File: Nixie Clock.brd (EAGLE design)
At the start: 197.2 x 106.7 mm, 149 parts, among them IC1_SECONDS_UNITS 4017N, IC2_SECONDS_TENS 4017N, IC3_MINUTES_UNITS 4017N, IC4_MINUTES_TENS 4017N, IC5_HOURS_UNITS 4017N, IC6_HOURS_TENS 4017N, IC7_AND 4081N, T0 MPSA42, T1 MPSA42, T10 MPSA42, T11 MPSA42, T12 MPSA42, T13 MPSA42, T14 MPSA42, T15 MPSA42, T16 MPSA42, T17 MPSA42, T18 MPSA42, T19 MPSA42, T2 MPSA42, T20 MPSA42, T21 MPSA42, T22 MPSA42, T23 MPSA42, T24 MPSA42, T25 MPSA42, T26 MPSA42, T27 MPSA42, T28 MPSA42, T29 MPSA42, T3 MPSA42, T30 MPSA42, T31 MPSA42, T32 MPSA42, T33 MPSA42, T34 MPSA42, T35 MPSA42, T36 MPSA42, T37 MPSA42, T38 MPSA42, T39 MPSA42, T4 MPSA42, T40 MPSA42, T41 MPSA42, T42 MPSA42, T43 MPSA42, T44 MPSA42, T5 MPSA42, T6 MPSA42, T7 MPSA42, T8 MPSA42, T9 MPSA42

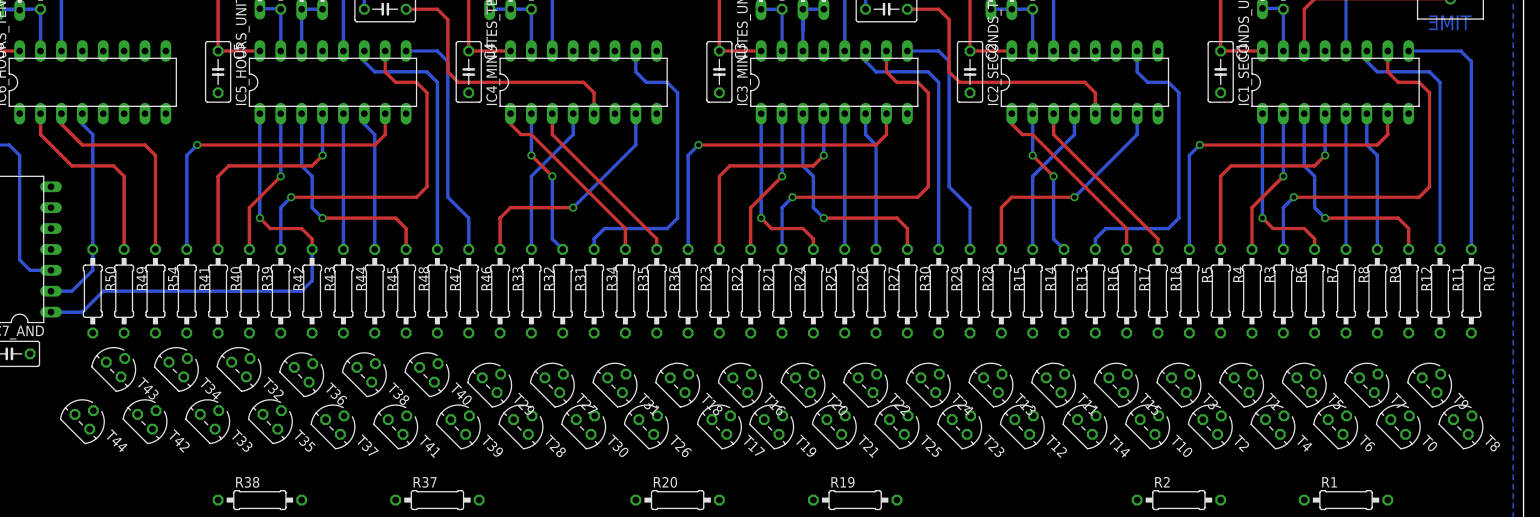
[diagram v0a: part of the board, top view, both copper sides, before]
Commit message: Rearrange transistors to avoid routes between the tubes' pins
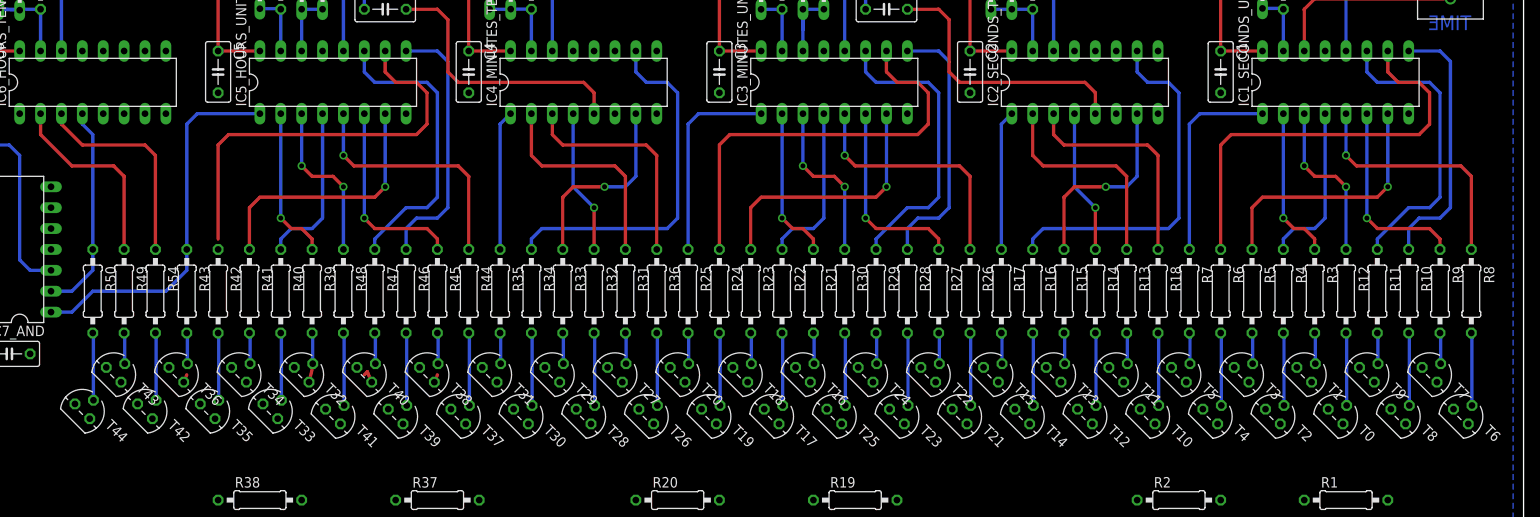
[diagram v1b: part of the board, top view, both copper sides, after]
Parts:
- moved T21 15.3 mm to (128.3, 33.0)
- moved T5 15.3 mm to (154.9, 38.1)
- moved T37 15.3 mm to (67.3, 33.0)
- moved T20 15.3 mm to (94.0, 38.1)
- moved T31 15.3 mm to (71.1, 38.1)
- moved T15 15.3 mm to (132.1, 38.1)
- moved T6 15.3 mm to (189.2, 33.0)
- moved R17 15.2 mm to (133.3, 48.3)
- moved R8 15.2 mm to (190.5, 48.3)
- moved R43 15.2 mm to (34.3, 48.3)
- moved R25 15.2 mm to (95.2, 48.3)
- moved R26 15.2 mm to (129.5, 48.3)
- moved R35 15.2 mm to (72.4, 48.3)
- moved R44 15.2 mm to (68.6, 48.3)
- moved T36 15.2 mm to (33.0, 38.1)
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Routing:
- net SEC_6: track 16.5 -> 30.3 mm, vias 0 -> 1
- net MIN_6: track 16.5 -> 30.3 mm, vias 0 -> 1
- net HOURS_6: track 16.5 -> 30.3 mm, vias 0 -> 1
- net HOURS_5: track 58.5 -> 45.8 mm, vias 1 -> 0
- net SEC_2: track 27.7 -> 18.8 mm, vias 1 -> 0
- net N$7: track 0.00 -> 8.84 mm
- net N$5: track 0.00 -> 8.84 mm
- net N$37: track 0.00 -> 8.84 mm
- net N$17: track 0.00 -> 8.84 mm
- net N$13: track 0.00 -> 8.84 mm
- net N$69: track 0.00 -> 8.84 mm
- net N$49: track 0.00 -> 8.84 mm
- net N$47: track 0.00 -> 8.84 mm
- net N$45: track 0.00 -> 8.84 mm
- net N$41: track 0.00 -> 8.84 mm
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
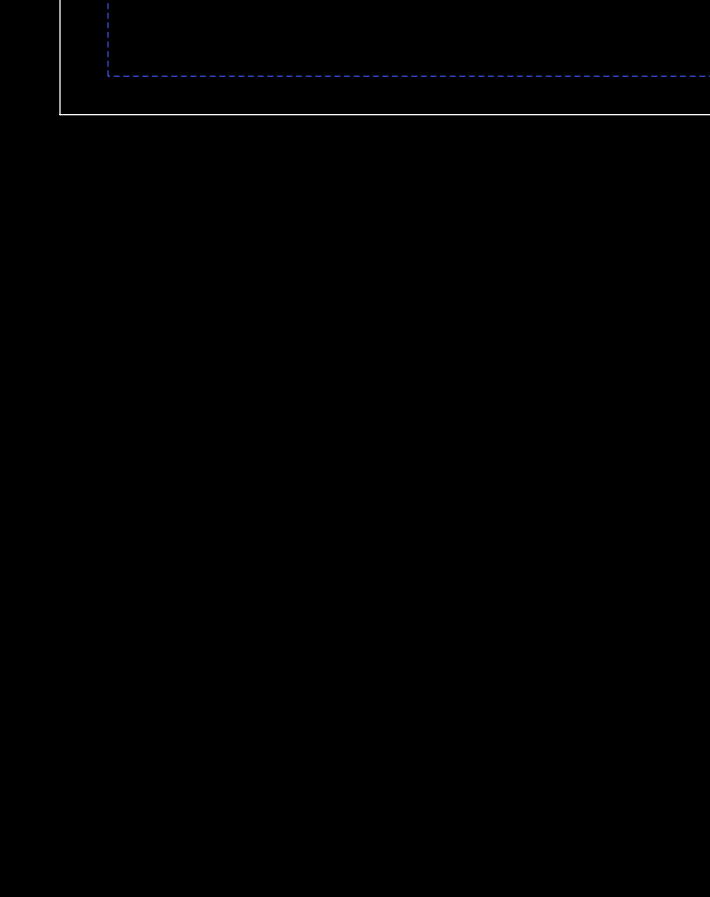
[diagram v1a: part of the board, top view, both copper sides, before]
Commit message: Add neon lamps
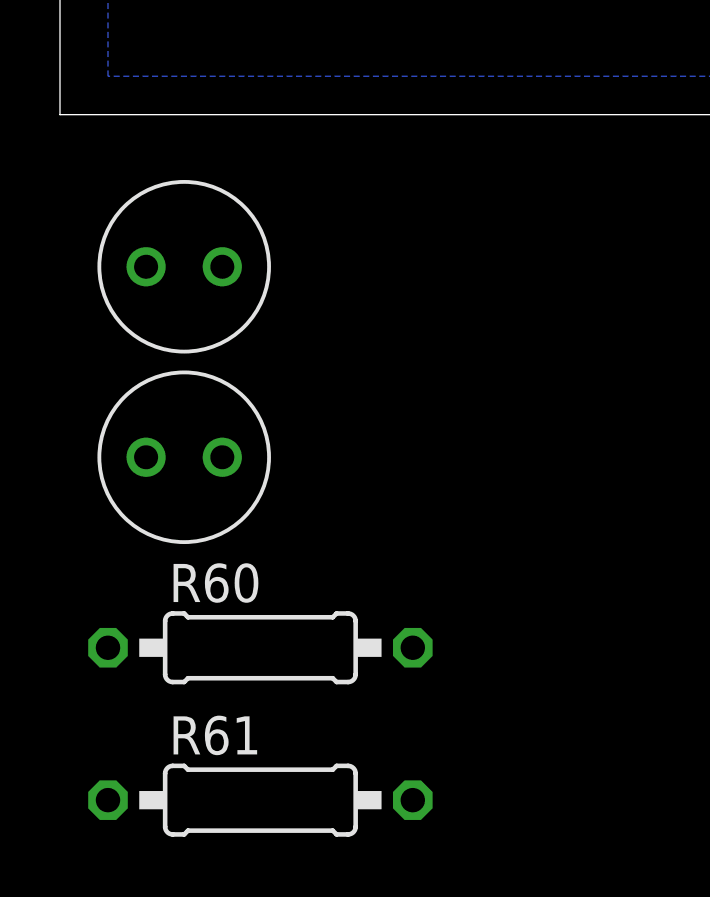
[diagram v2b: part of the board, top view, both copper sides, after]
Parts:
- added LMP1, LMP2: NE2H, PGT:NEON_LAMP_0.1_INCH
- added R60, R61: 33.3k, resistor:0207/10
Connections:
- new net N$107: LMP2.P$1, R61.2
- new net N$108: LMP1.P$1, R60.2
- net GND: now also LMP1.P$2, LMP2.P$2
- net VHIGH: now also R60.1, R61.1

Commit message: All Routed \o/
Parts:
- R1, R19, R2, R20, R37, R38, R60, R61: device resistor:0207/10 -> resistor:0207/2V
- moved CON_HIGH_VOLTAGE 176.7 mm to (12.7, 34.3), turned to 180 degrees
- moved R61 129.5 mm to (127.0, 24.1), turned to 270 degrees
- moved LMP2 125.3 mm to (127.0, 11.4), turned to 270 degrees
- moved R60 80.4 mm to (74.9, 24.1), turned to 270 degrees
- moved LMP1 73.0 mm to (74.9, 11.4), turned to 270 degrees
- moved R2 12.8 mm to (142.2, 24.1), turned to 90 degrees
- moved R1 11.5 mm to (163.8, 24.1), turned to 90 degrees
- moved SECONDS_TENS 7.62 mm to (142.2, 11.4)
- moved SECONDS_UNITS 6.35 mm to (163.8, 11.4)
- moved R37 5.24 mm to (59.7, 24.1), turned to 90 degrees
- moved R38 5.24 mm to (38.1, 24.1), turned to 90 degrees
- moved R20 4.02 mm to (90.2, 24.1), turned to 90 degrees
- moved R19 4.02 mm to (111.8, 24.1), turned to 90 degrees
- moved C9 2.54 mm to (12.7, 43.2)
- moved IC7_AND 2.54 mm to (14.0, 55.9)
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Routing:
- net VHIGH: track 0.00 -> 154.5 mm
- net N$95: track 0.97 -> 46.4 mm
- net N$57: track 0.00 -> 43.5 mm
- net N$63: track 0.00 -> 42.2 mm
- net N$30: track 0.00 -> 42.1 mm
- net N$23: track 0.00 -> 41.6 mm
- net N$31: track 0.00 -> 41.5 mm
- net N$79: track 0.00 -> 40.3 mm
- net N$64: track 0.00 -> 37.4 mm
- net N$87: track 0.00 -> 35.9 mm
- net N$96: track 0.00 -> 35.8 mm
- net N$88: track 0.97 -> 36.7 mm
- net N$94: track 0.00 -> 35.0 mm
- net N$93: track 0.00 -> 33.6 mm
- net N$28: track 0.00 -> 33.6 mm
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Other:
- board text added: "HIGH"
